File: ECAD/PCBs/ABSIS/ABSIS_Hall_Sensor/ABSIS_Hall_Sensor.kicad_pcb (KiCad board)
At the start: 2 copper layers, 16 x 44 mm, 10 parts, among them J1 IN, J2 OUT, U1 AS5045B

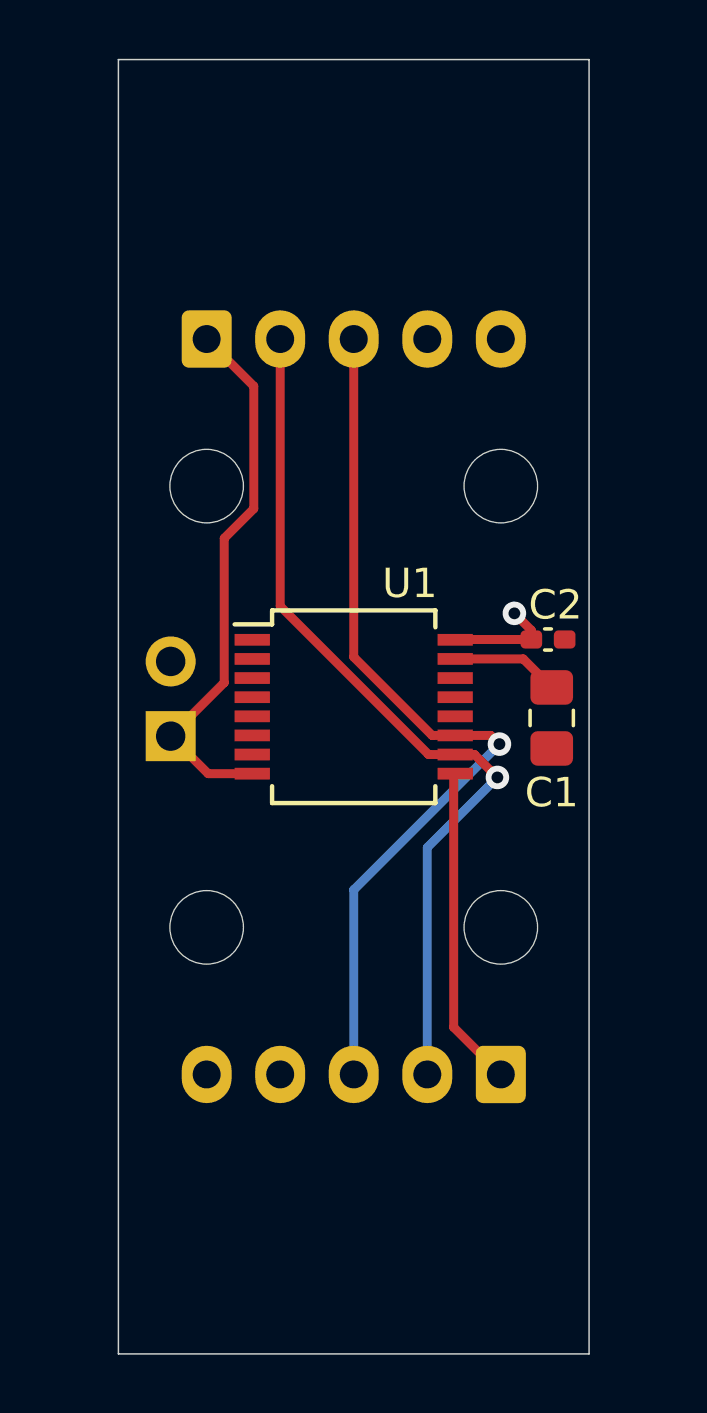
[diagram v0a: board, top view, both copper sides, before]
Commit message: Roll Sensor Redesign WIP
Hall Sensor Design Complete
Roll Sensor structure redesign WIP
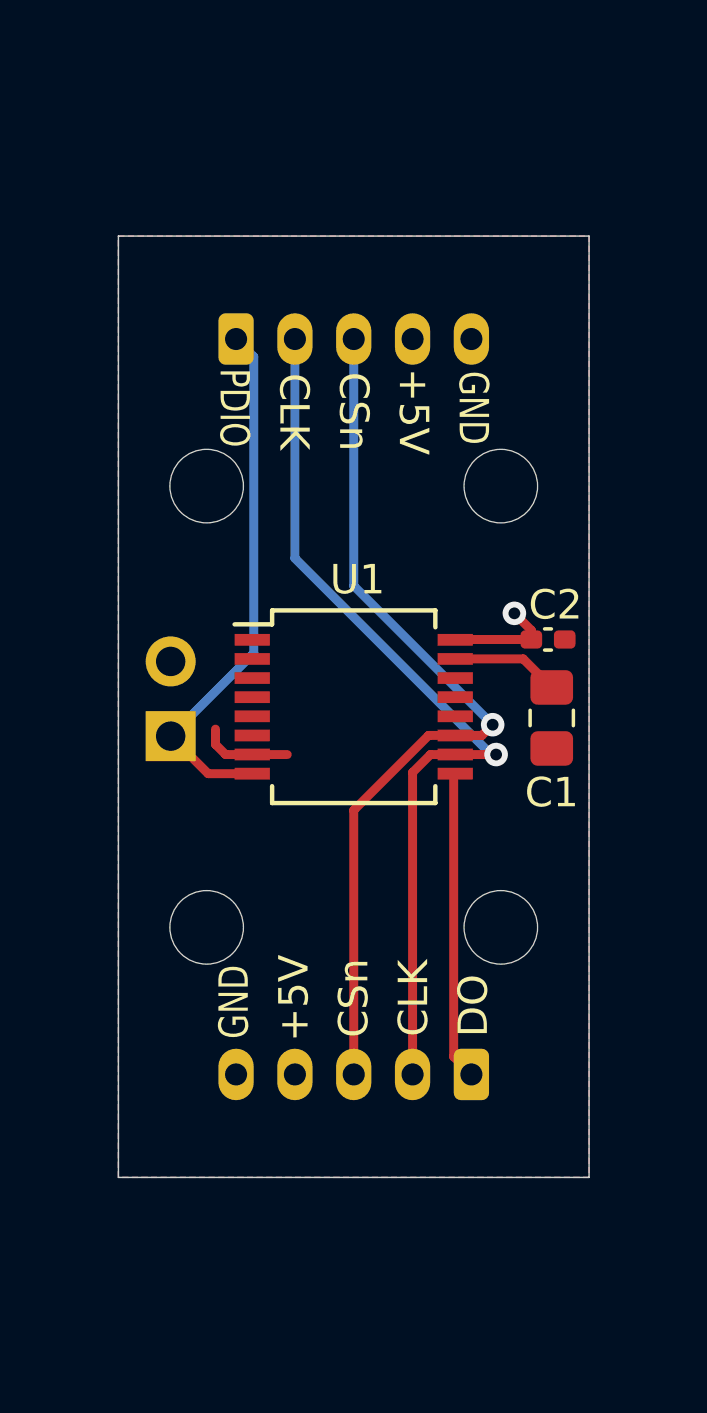
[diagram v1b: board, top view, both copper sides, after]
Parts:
- J1, J2: footprint Connector_JST:JST_XH_S5B-XH-A_1x05_P2.50mm_Horizontal -> Connector_JST:JST_PH_B5B-PH-K_1x05_P2.00mm_Vertical
- moved J1 1.00 mm to (176.8, 110.8)
- moved J2 1.00 mm to (168.8, 85.8)
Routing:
- net GND: track 0.00 -> 3.10 mm
- added copper zone on B.Cu, net +5V
- added copper zone on F.Cu, net GND
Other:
- board size 16 x 44 mm -> 16 x 32 mm
- board text added: "+5V"
- board text added: "ABSIS HALL"
- board text added: "CLK"
- board text added: "CSn"
- board text added: "DO"
- board text added: "GND"
- board text added: "PDIO"
- board text added: "SENSOR"

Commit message: Redesigned Hall Sensor with MT6825 18 bit sensor.
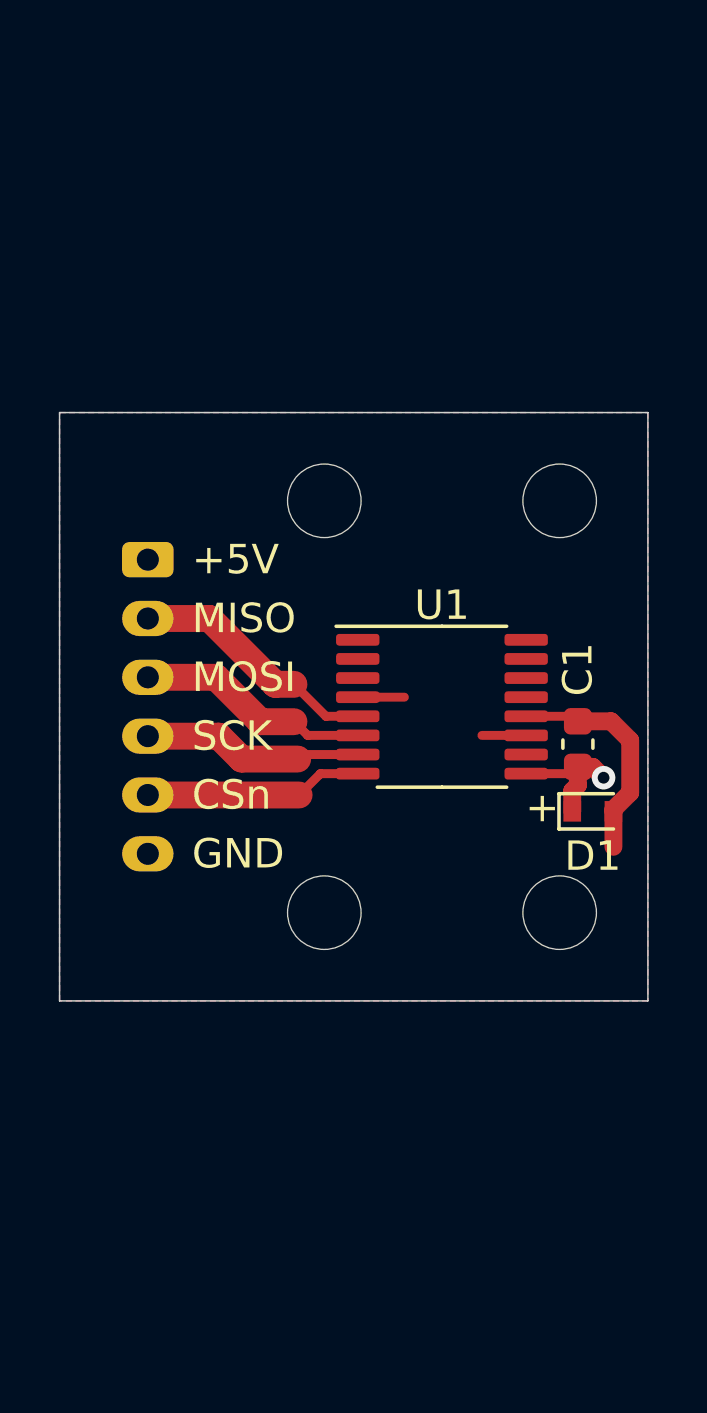
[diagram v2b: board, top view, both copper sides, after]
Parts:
- removed C2: 100nF, Capacitor_SMD:C_0402_1005Metric_Pad0.74x0.62mm_HandSolder
- removed J2: OUT, Connector_JST:JST_PH_B5B-PH-K_1x05_P2.00mm_Vertical
- removed JP1: LAST/ONLY, Connector_PinHeader_2.54mm:PinHeader_1x02_P2.54mm_Vertical
- added D1: ESD5Z5V0, Diode_SMD:D_SOD-523, F.Cu at (181.0, 101.9)
- C1: value 10uF -> 0.1uF; footprint Capacitor_SMD:C_0805_2012Metric_Pad1.18x1.45mm_HandSolder -> Capacitor_SMD:C_0603_1608Metric
- J1: footprint Connector_JST:JST_PH_B5B-PH-K_1x05_P2.00mm_Vertical -> Connector_JST:JST_PH_B6B-PH-K_1x06_P2.00mm_Vertical
- U1: value AS5045B -> MT6825GT; footprint Package_SO:SSOP-16_5.3x6.2mm_P0.65mm -> Package_SO:TSSOP-16_4.4x5mm_P0.65mm
- moved J1 20.7 mm to (165.8, 93.3), turned to 270 degrees
- moved H2 15.7 mm to (171.8, 105.3)
- moved H4 14.6 mm to (179.8, 91.3)
- moved H3 12.0 mm to (179.8, 105.3)
- moved H1 4.03 mm to (171.8, 91.3)
- moved U1 3.00 mm to (175.8, 98.3)
- moved C1 1.26 mm to (180.5, 99.6)
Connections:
- C1 pad 1: GND -> +5V
- C1 pad 2: Net-(C1-Pad2) -> GND
- J1 pad 1: /DO -> +5V
- J1 pad 2: /CLK -> /MISO
- J1 pad 3: /CSn -> /MOSI
- J1 pad 4: +5V -> /SCK
- J1 pad 5: GND -> /CSN
- U1 pad 10: /CLK -> Net-(U1-Pad10)
- U1 pad 11: /CSn -> GND
- U1 pad 12: Net-(U1-Pad12) -> GND
- U1 pad 15: Net-(C1-Pad2) -> Net-(U1-Pad15)
- U1 pad 16: +5V -> Net-(U1-Pad16)
- U1 pad 4: Net-(U1-Pad4) -> GND
- U1 pad 5: Net-(U1-Pad5) -> /MISO
- U1 pad 6: Net-(U1-Pad6) -> /MOSI
- U1 pad 7: GND -> /SCK
- U1 pad 8: /PDIO -> /CSN
- U1 pad 9: /DO -> +5V
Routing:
- net /CLK: track 30.4 -> 0.00 mm, vias 1 -> 0
- net /CSn: track 30.0 -> 0.00 mm, vias 1 -> 0
- net /PDIO: track 18.2 -> 0.00 mm
- net /DO: track 10.5 -> 0.00 mm
- net /MISO: track 0.00 -> 8.51 mm
- net /MOSI: track 0.00 -> 7.96 mm
- net GND: track 3.10 -> 10.8 mm
- net /SCK: track 0.00 -> 7.52 mm
- net /CSN: track 0.00 -> 7.44 mm
- net Net-(C1-Pad2): track 3.68 -> 0.00 mm
- net +5V: track 3.72 -> 4.47 mm
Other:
- board size 16 x 32 mm -> 20 x 20 mm
- board text added: "+"
- board text added: "0°"
- board text added: "1"
- board text added: "ABSIS HALL SENSOR"
- board text added: "CC BY-NC-SA"
- board text added: "MISO"
- board text added: "MOSI"
- board text added: "OPENHORNET.COM"
- board text added: "REV: 2"
- board text added: "SCK"
- board text added: "THIS SIDE AWAY FROM MAGNET"
- board text removed: "ABSIS HALL"
- board text removed: "CLK"
- board text removed: "DO"
- board text removed: "PDIO"
- board text removed: "SENSOR"

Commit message: Stick WIP
Sensor converted to RA connector.
New sensor integrated in roll and pitch.
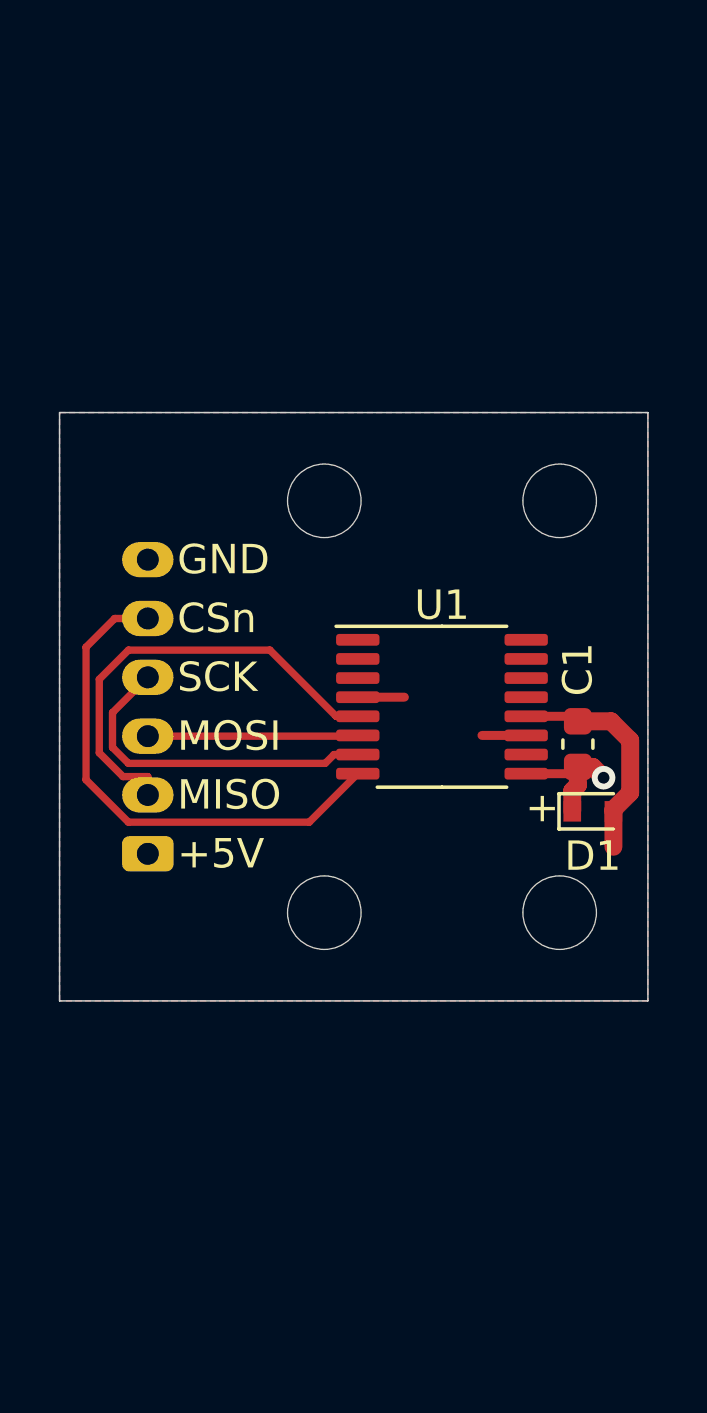
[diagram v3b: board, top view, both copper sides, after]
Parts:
- J1: footprint Connector_JST:JST_PH_B6B-PH-K_1x06_P2.00mm_Vertical -> Connector_JST:JST_PH_S6B-PH-K_1x06_P2.00mm_Horizontal
- moved J1 10.0 mm to (165.8, 103.3), turned to 90 degrees
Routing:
- net /CSN: track 7.44 -> 17.5 mm
- net /MISO: track 8.51 -> 15.2 mm
- net /SCK: track 7.52 -> 11.6 mm
- net /MOSI: track 7.96 -> 7.15 mm

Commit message: KiCad 5 to 6 Transition - ABSIS_Hall_Sensor
1:  OH Nomenclature:  - No change to name

2:  Added "Legacy" folder:  Used to store all files that are no longer being used and are associated with KiCad 5 and older.

3:  Moved old BOM/CPL files to Legacy folder until new manufacturing files are verified.

4:  Added:  STEP File
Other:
- net class Default removed
